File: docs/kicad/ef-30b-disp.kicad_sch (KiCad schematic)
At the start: 20 parts, among them J1 IC16, J2 IC16

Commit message: Added the complete kicad project.
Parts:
- added JP1: Addr Sel, symbol Jumper:Jumper_3_Bridged12
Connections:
- net at U1.27 (GP21): now also JP1.3 (B)
- net at U1.28 (GND): now also JP1.2 (C)
- net at U1.29 (GP22): now also JP1.1 (A)
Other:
- note added: "EF30B Display Board"
- note removed: "EF30B Control Board"
- title: EF-30B-DISP V11 2017-10-8 -> EF30B-disp I2C Driver
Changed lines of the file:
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@@
   (paper "USLetter")
   (title_block
-    (title "EF-30B-DISP V11 2017-10-8")
+    (title "EF30B-disp I2C Driver")
     (date "2023-12-03")
+    (comment 1 "For the EF-30B-DISP V11 2017-10-8 display board")
   )
   (junction (at 30.48 83.82) (diameter 0) (color 0 0 0 0)
@@
     (stroke (width 0) (type default))
   )
+  (wire (pts (xy 58.42 128.27) (xy 62.23 128.27))
+    (stroke (width 0) (type default))
+  )
   (wire (pts (xy 110.49 135.89) (xy 110.49 161.29))
     (stroke (width 0) (type default))
@@
     (stroke (width 0) (type default))
   )
+  (wire (pts (xy 55.88 134.62) (xy 58.42 134.62))
+    (stroke (width 0) (type default))
+  )
   (wire (pts (xy 43.18 48.26) (xy 27.94 48.26))
     (stroke (width 0) (type default))
@@
     (stroke (width 0) (type default))
   )
+  (wire (pts (xy 55.88 132.08) (xy 58.42 132.08))
+    (stroke (width 0) (type default))
+  )
   (wire (pts (xy 27.94 78.74) (xy 48.26 78.74))
     (stroke (width 0) (type default))
@@
     (stroke (width 0) (type default))
   )
+  (wire (pts (xy 58.42 137.16) (xy 58.42 140.97))
+    (stroke (width 0) (type default))
+  )
   (wire (pts (xy 219.71 50.8) (xy 175.26 50.8))
     (stroke (width 0) (type default))
   )
-  (wire (pts (xy 55.88 121.92) (xy 66.04 121.92))
+  (wire (pts (xy 55.88 121.92) (xy 69.85 121.92))
+    (stroke (width 0) (type default))
+  )
+  (wire (pts (xy 58.42 132.08) (xy 58.42 128.27))
     (stroke (width 0) (type default))
   )
@@
     (stroke (width 0) (type default))
   )
+  (wire (pts (xy 55.88 137.16) (xy 58.42 137.16))
+    (stroke (width 0) (type default))
+  )
   (wire (pts (xy 30.48 144.78) (xy 16.51 144.78))
     (stroke (width 0) (type default))
@@
     (stroke (width 0) (type default))
   )
+  (wire (pts (xy 58.42 140.97) (xy 62.23 140.97))
+    (stroke (width 0) (type default))
+  )
   (wire (pts (xy 123.19 33.02) (xy 180.34 33.02))
     (stroke (width 0) (type default))
@@
   )
   (wire (pts (xy 175.26 71.12) (xy 175.26 63.5))
-    (stroke (width 0) (type default))
-  )
-  (wire (pts (xy 66.04 121.92) (xy 66.04 123.19))
     (stroke (width 0) (type default))
   )
@@
     (effects (font (size 1.27 1.27)) (justify left bottom))
   )
-  (text "EF30B Control Board" (at 194.31 104.14 0)
+  (text "EF30B Display Board" (at 194.31 104.14 0)
     (effects (font (size 1.27 1.27)) (justify left bottom))
   )
@@
     )
   )
+  (symbol (lib_id "Jumper:Jumper_3_Bridged12") (at 62.23 134.62 270) (unit 1)
+    (in_bom yes) (on_board yes) (dnp no) (fields_autoplaced)
+    (property "Reference" "JP1" (at 64.77 133.35 90)
+      (effects (font (size 1.27 1.27)) (justify left))
+    )
+    (property "Value" "Addr Sel" (at 64.77 135.89 90)
+      (effects (font (size 1.27 1.27)) (justify left))
+    )
+    (property "Footprint" "" (at 62.23 134.62 0)
+      (effects (font (size 1.27 1.27)) hide)
+    )
+    (property "Datasheet" "~" (at 62.23 134.62 0)
+      (effects (font (size 1.27 1.27)) hide)
+    )
+    (pin "3")
+    (pin "2")
+    (pin "1")
+    (instances
+      (project "ef-30b-disp"
+        (path "/80e01998-b851-47c3-8e60-9cd21717e5b8"
+          (reference "JP1") (unit 1)
+        )
+      )
+    )
+  )
   (symbol (lib_id "power:GND") (at 147.32 26.67 0) (unit 1)
     (in_bom yes) (on_board yes) (dnp no) (fields_autoplaced)
@@
     )
   )
-  (symbol (lib_id "power:GND") (at 66.04 123.19 0) (unit 1)
-    (in_bom yes) (on_board yes) (dnp no) (fields_autoplaced)
-    (property "Reference" "#PWR02" (at 66.04 129.54 0)
-      (effects (font (size 1.27 1.27)) hide)
-    )
-    (property "Value" "GND" (at 66.04 128.27 0)
-      (effects (font (size 1.27 1.27)))
-    )
-    (property "Footprint" "" (at 66.04 123.19 0)
-      (effects (font (size 1.27 1.27)) hide)
-    )
-    (property "Datasheet" "" (at 66.04 123.19 0)
-      (effects (font (size 1.27 1.27)) hide)
-    )
+  (symbol (lib_id "power:GND") (at 69.85 121.92 0) (unit 1)
+    (in_bom yes) (on_board yes) (dnp no) (fields_autoplaced)
+    (property "Reference" "#PWR02" (at 69.85 128.27 0)
+      (effects (font (size 1.27 1.27)) hide)
+    )
+    (property "Value" "GND" (at 69.85 127 0)
+      (effects (font (size 1.27 1.27)))
+    )
+    (property "Footprint" "" (at 69.85 121.92 0)
+      (effects (font (size 1.27 1.27)) hide)
+    )
+    (property "Datasheet" "" (at 69.85 121.92 0)
+      (effects (font (size 1.27 1.27)) hide)
+    )

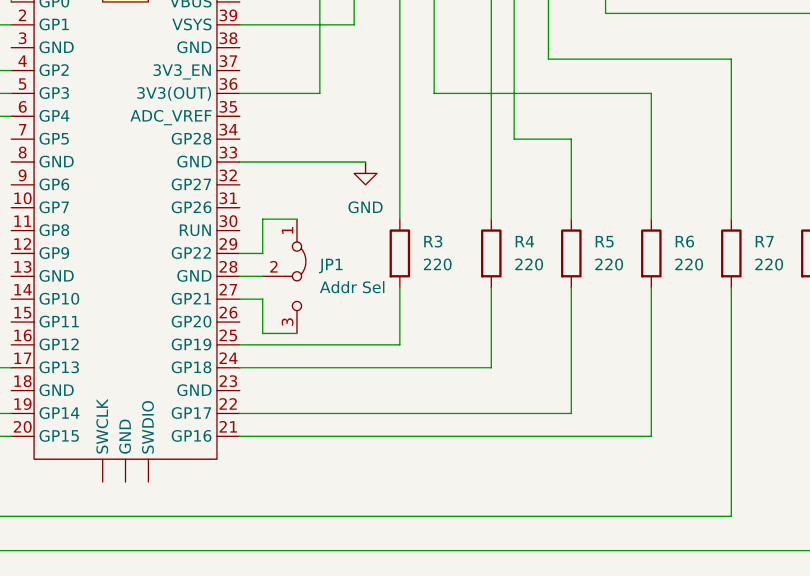
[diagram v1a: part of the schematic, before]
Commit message: Added jumpers to the board for VSYS and GND. Updated the shcematic and wiring table.
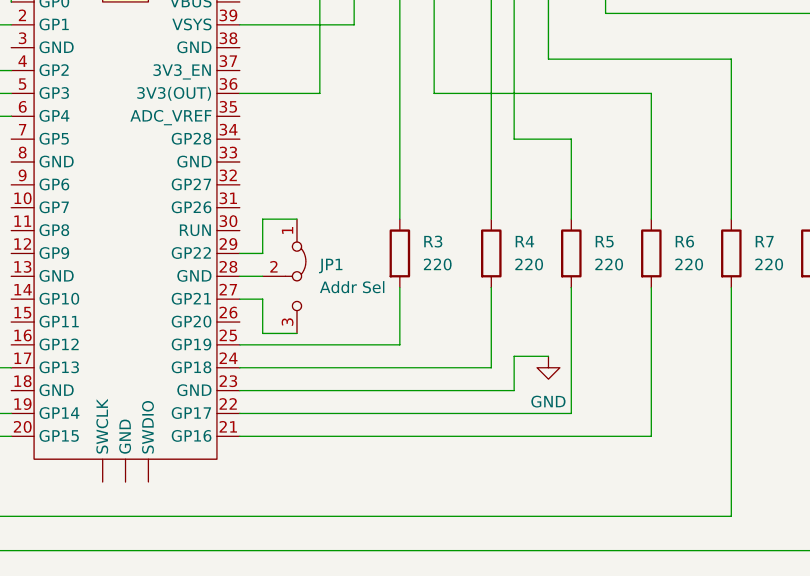
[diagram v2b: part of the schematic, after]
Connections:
- net GND: now also U1.23 (GND); no longer U1.33 (GND)
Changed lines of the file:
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@@
+    (stroke (width 0) (type default))
+  )
+  (wire (pts (xy 55.88 147.32) (xy 86.36 147.32))
     (stroke (width 0) (type default))
   )
@@
     (stroke (width 0) (type default))
   )
-  (wire (pts (xy 55.88 121.92) (xy 69.85 121.92))
-    (stroke (width 0) (type default))
-  )
   (wire (pts (xy 58.42 132.08) (xy 58.42 128.27))
     (stroke (width 0) (type default))
   )
+  (wire (pts (xy 86.36 143.51) (xy 90.17 143.51))
+    (stroke (width 0) (type default))
+  )
   (wire (pts (xy 68.58 106.68) (xy 55.88 106.68))
     (stroke (width 0) (type default))
@@
   )
   (wire (pts (xy 157.48 58.42) (xy 154.94 58.42))
+    (stroke (width 0) (type default))
+  )
+  (wire (pts (xy 86.36 147.32) (xy 86.36 143.51))
     (stroke (width 0) (type default))
   )
@@
     )
   )
-  (symbol (lib_id "power:GND") (at 69.85 121.92 0) (unit 1)
-    (in_bom yes) (on_board yes) (dnp no) (fields_autoplaced)
-    (property "Reference" "#PWR02" (at 69.85 128.27 0)
-      (effects (font (size 1.27 1.27)) hide)
-    )
-    (property "Value" "GND" (at 69.85 127 0)
-      (effects (font (size 1.27 1.27)))
-    )
-    (property "Footprint" "" (at 69.85 121.92 0)
-      (effects (font (size 1.27 1.27)) hide)
-    )
-    (property "Datasheet" "" (at 69.85 121.92 0)
-      (effects (font (size 1.27 1.27)) hide)
-    )
+  (symbol (lib_id "power:GND") (at 90.17 143.51 0) (unit 1)
+    (in_bom yes) (on_board yes) (dnp no) (fields_autoplaced)
+    (property "Reference" "#PWR02" (at 90.17 149.86 0)
+      (effects (font (size 1.27 1.27)) hide)
+    )
+    (property "Value" "GND" (at 90.17 148.59 0)
+      (effects (font (size 1.27 1.27)))
+    )
+    (property "Footprint" "" (at 90.17 143.51 0)
+      (effects (font (size 1.27 1.27)) hide)
+    )
+    (property "Datasheet" "" (at 90.17 143.51 0)
+      (effects (font (size 1.27 1.27)) hide)
+    )
